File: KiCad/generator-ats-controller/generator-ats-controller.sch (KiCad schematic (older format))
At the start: 20 parts

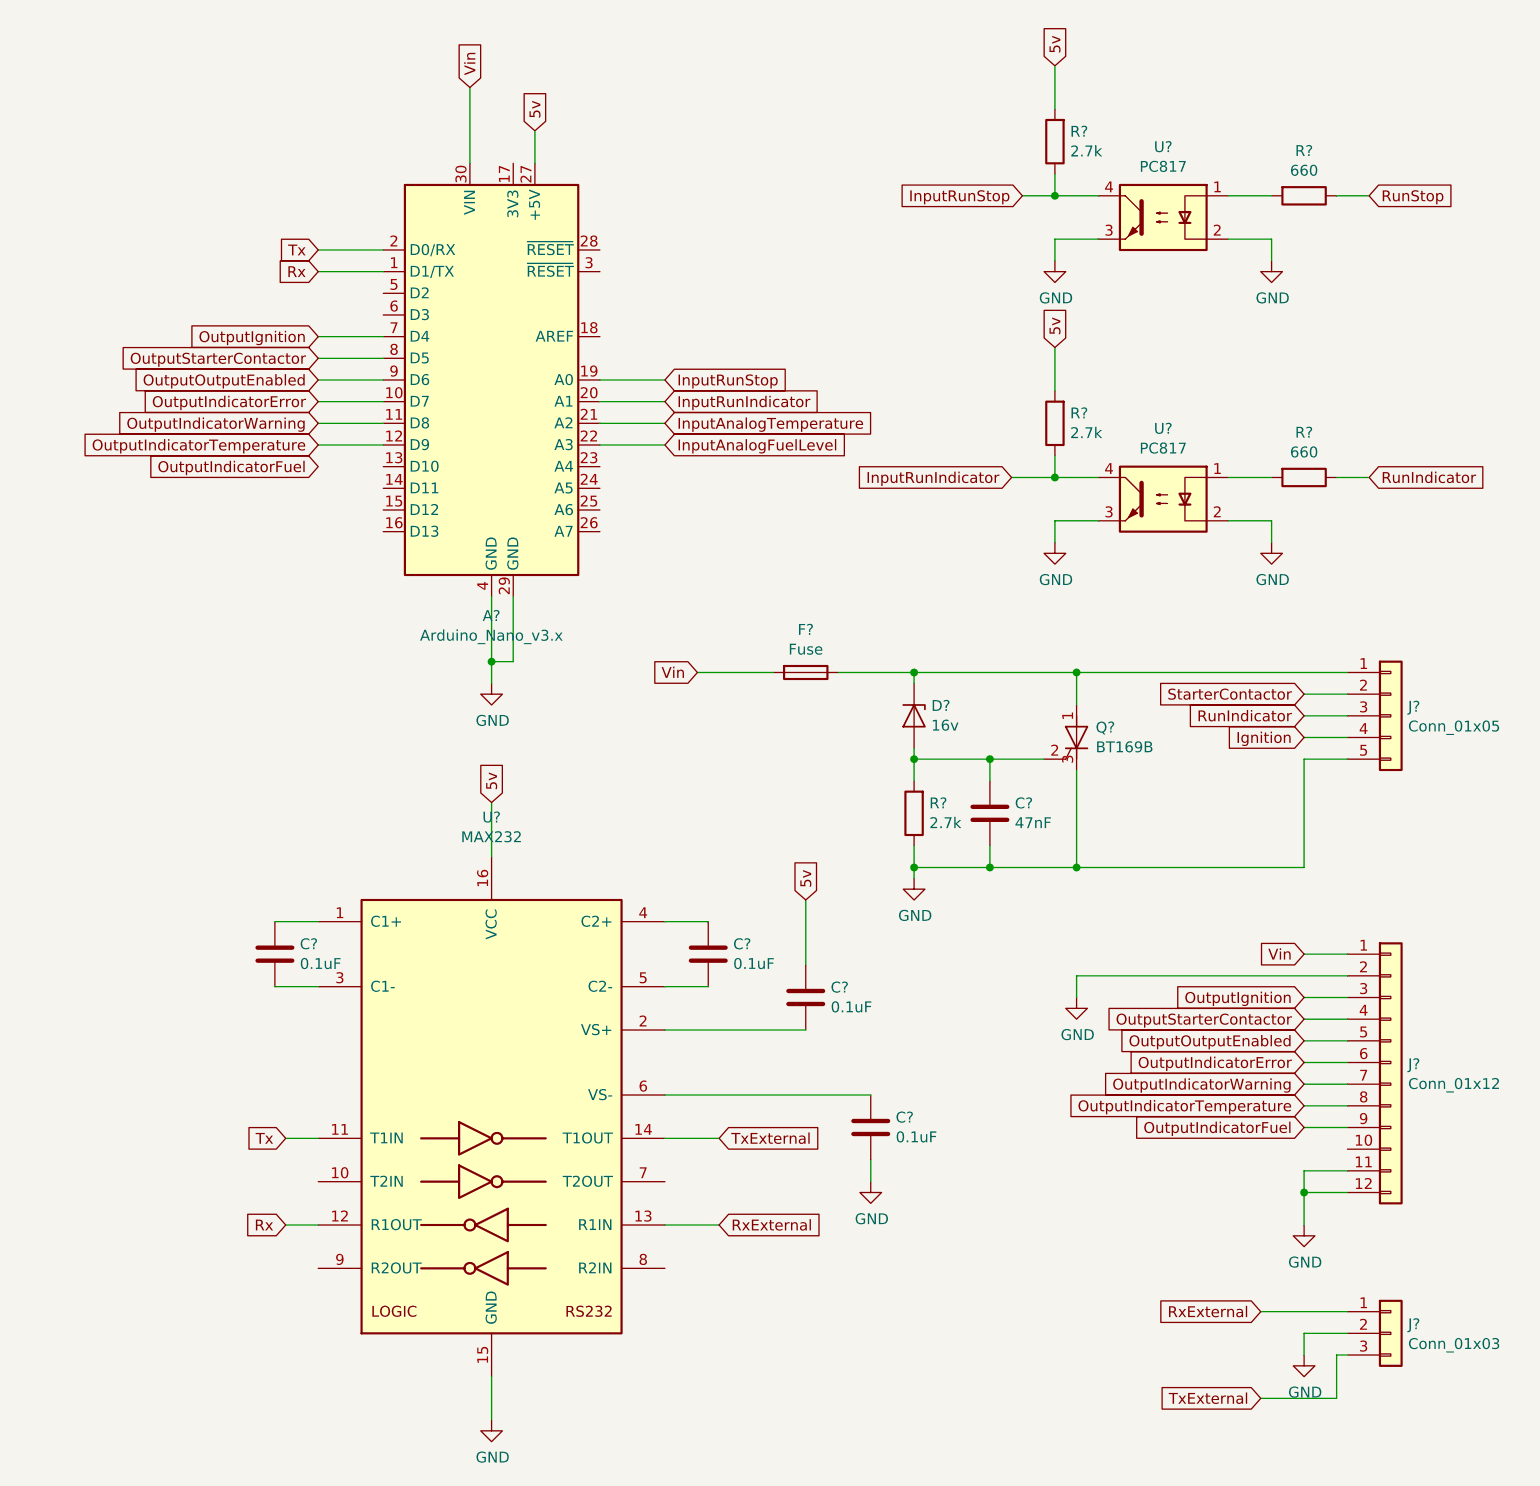
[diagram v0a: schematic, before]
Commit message: * Correct errors in schematic, largely around the MAX232
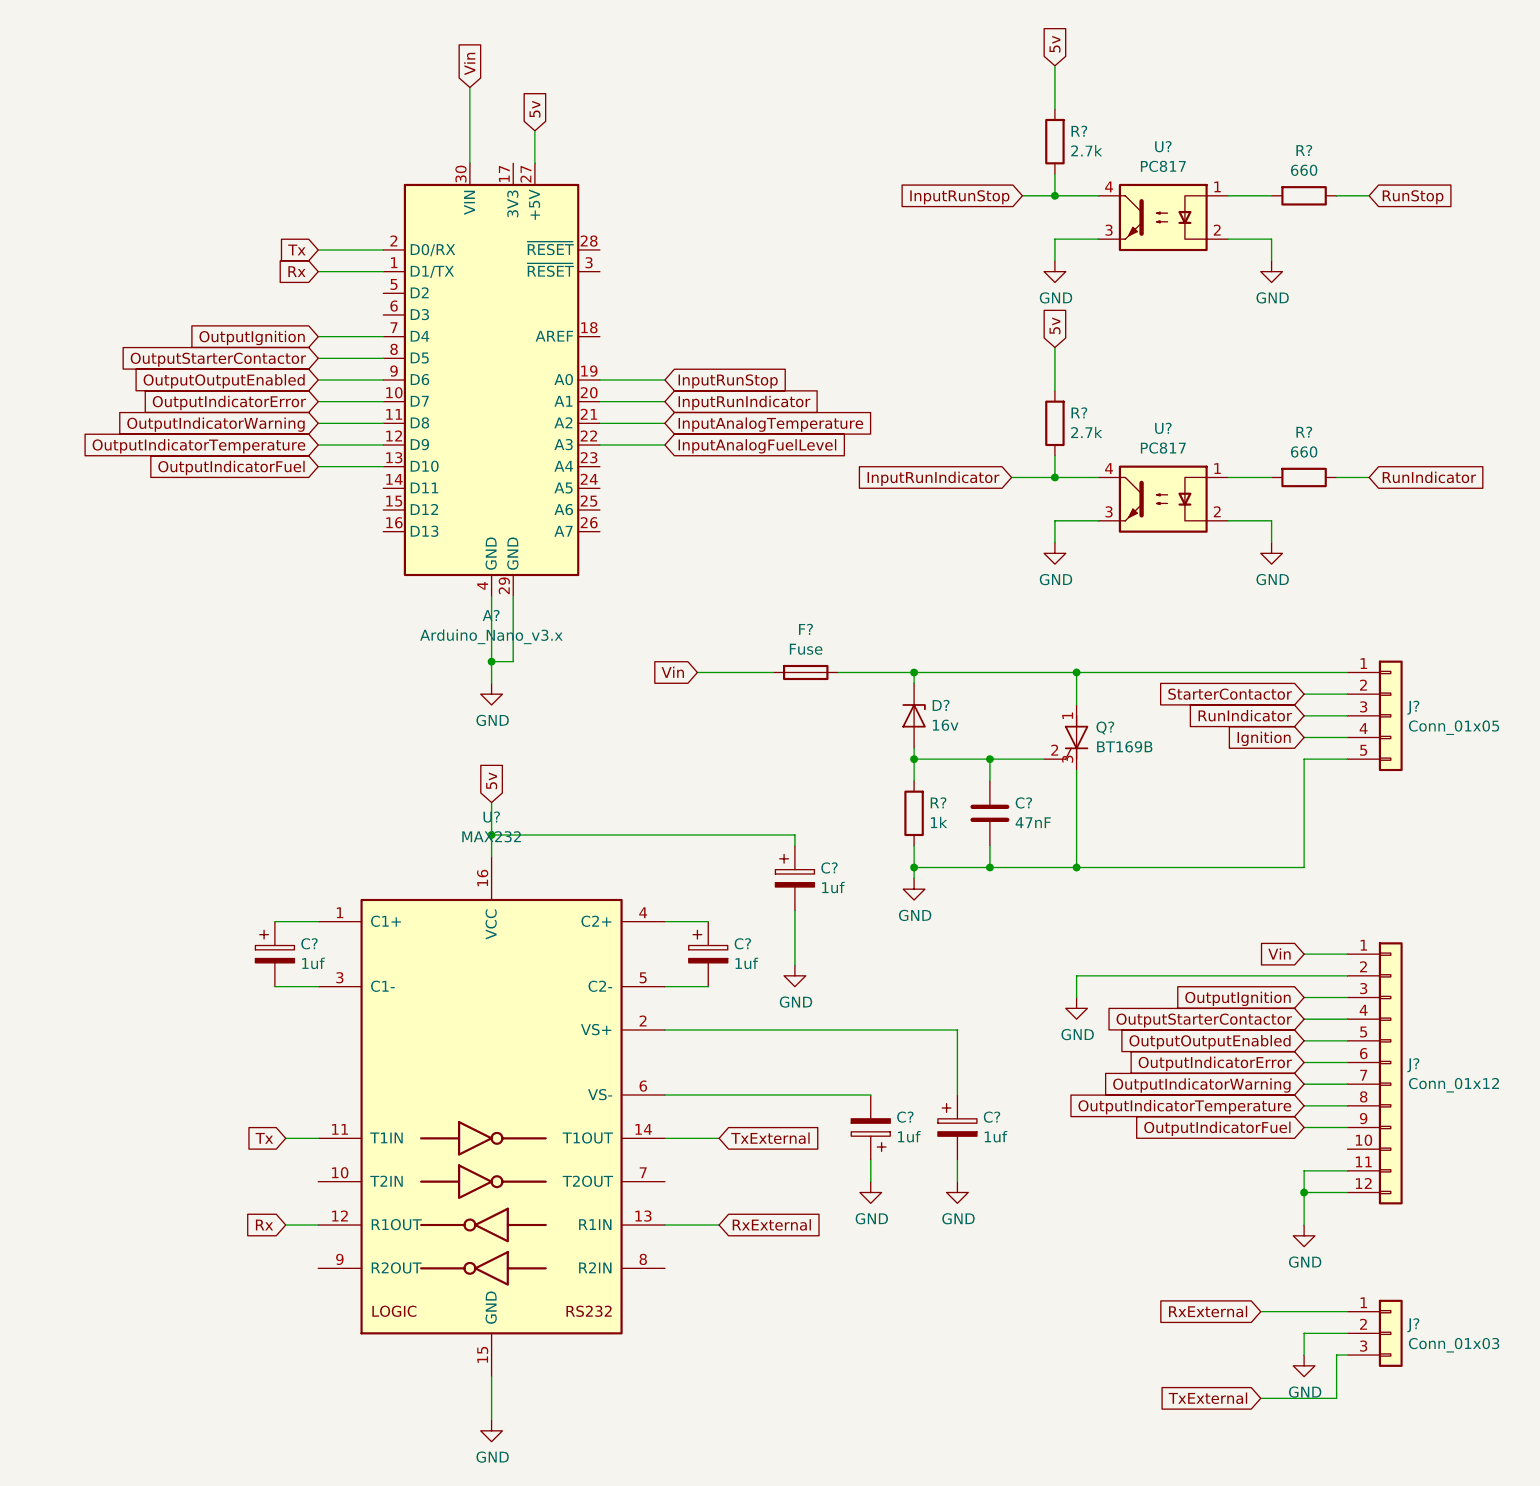
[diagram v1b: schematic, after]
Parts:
- removed C? (x4): 0.1uF, symbol Device:C
- added C? (x5): 1uf, symbol Device:CP
- R?: value 2.7k -> 1k
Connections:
- net 5v: now also C?.1
- net GND: now also C?.1, C?.2, C?.2
- net OutputIndicatorFuel: now also A?.13 (D10)
- net at U?.1 (C1+): now also C?.1
- net at U?.2 (VS+): now also C?.1
- net at U?.3 (C1-): now also C?.2
- net at U?.4 (C2+): now also C?.1
- net at U?.5 (C2-): now also C?.2
- net at U?.6 (VS-): now also C?.2
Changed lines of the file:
@@
-	1    0    0    -1
-$EndComp
-$Comp
-L Device:C C?
-U 1 1 5F2662F8
-P 1550 5100
-F 0 "C?" H 1665 5146 50  0000 L CNN
-F 1 "0.1uF" H 1665 5055 50  0000 L CNN
-F 2 "" H 1588 4950 50  0001 C CNN
-F 3 "~" H 1550 5100 50  0001 C CNN
-	1    1550 5100
-	1    0    0    -1
-$EndComp
-$Comp
-L Device:C C?
-U 1 1 5F2691ED
-P 3550 5100
-F 0 "C?" H 3665 5146 50  0000 L CNN
-F 1 "0.1uF" H 3665 5055 50  0000 L CNN
-F 2 "" H 3588 4950 50  0001 C CNN
-F 3 "~" H 3550 5100 50  0001 C CNN
-	1    3550 5100
-	1    0    0    -1
-$EndComp
-$Comp
-L Device:C C?
-U 1 1 5F269678
-P 4000 5300
-F 0 "C?" H 4115 5346 50  0000 L CNN
-F 1 "0.1uF" H 4115 5255 50  0000 L CNN
-F 2 "" H 4038 5150 50  0001 C CNN
-F 3 "~" H 4000 5300 50  0001 C CNN
-	1    4000 5300
-	1    0    0    -1
-$EndComp
-$Comp
-L Device:C C?
-U 1 1 5F269EC4
-P 4300 5900
-F 0 "C?" H 4415 5946 50  0000 L CNN
-F 1 "0.1uF" H 4415 5855 50  0000 L CNN
-F 2 "" H 4338 5750 50  0001 C CNN
-F 3 "~" H 4300 5900 50  0001 C CNN
-	1    4300 5900
 	1    0    0    -1
 $EndComp
@@
 Wire Wire Line
 	2450 1450 2450 1100
-Text GLabel 4000 4850 1    50   Input ~ 0
-5v
 $Comp
 L power:GND #PWR?
@@
 	1    0    0    -1
 $EndComp
-Wire Wire Line
-	3350 5450 4000 5450
 Text GLabel 1750 1850 0    50   Input ~ 0
 Tx
@@
 5v
 Wire Wire Line
-	2550 4400 2550 4650
+	2550 4400 2550 4550
 Wire Wire Line
 	6100 7150 6450 7150
@@
 P 4500 4450
 F 0 "R?" H 4430 4404 50  0000 R CNN
-F 1 "2.7k" H 4430 4495 50  0000 R CNN
+F 1 "1k" H 4430 4495 50  0000 R CNN
 F 2 "" V 4430 4450 50  0001 C CNN
 F 3 "~" H 4500 4450 50  0001 C CNN
@@
 Wire Wire Line
 	4850 4200 5100 4200
-Wire Wire Line
-	4000 4850 4000 5150
 $Comp
 L Connector_Generic:Conn_01x03 J?
@@
 Text GLabel 6100 6750 0    50   Input ~ 0
 RxExternal
+$Comp
+L power:GND #PWR?
+U 1 1 5F4B4680
+P 4700 6150
+F 0 "#PWR?" H 4700 5900 50  0001 C CNN
+F 1 "GND" H 4705 5977 50  0000 C CNN
+F 2 "" H 4700 6150 50  0001 C CNN
+F 3 "" H 4700 6150 50  0001 C CNN
+	1    4700 6150
+	1    0    0    -1
+$EndComp
+Wire Wire Line
+	4700 6150 4700 6050
+Wire Wire Line
+	4700 5750 4700 5450
+Wire Wire Line
+	3350 5450 4700 5450
+$Comp
+L Device:CP C?
+U 1 1 5F4BEB4E
+P 1550 5100
+F 0 "C?" H 1668 5146 50  0000 L CNN
+F 1 "1uf" H 1668 5055 50  0000 L CNN
+F 2 "" H 1588 4950 50  0001 C CNN
+F 3 "~" H 1550 5100 50  0001 C CNN
+	1    1550 5100
+	1    0    0    -1
+$EndComp
+$Comp
+L Device:CP C?
+U 1 1 5F4C0CED
+P 3550 5100
+F 0 "C?" H 3668 5146 50  0000 L CNN
+F 1 "1uf" H 3668 5055 50  0000 L CNN
+F 2 "" H 3588 4950 50  0001 C CNN
+F 3 "~" H 3550 5100 50  0001 C CNN
+	1    3550 5100
+	1    0    0    -1
+$EndComp
+$Comp
+L Device:CP C?
+U 1 1 5F4C10F1
+P 4700 5900
+F 0 "C?" H 4818 5946 50  0000 L CNN
+F 1 "1uf" H 4818 5855 50  0000 L CNN
+F 2 "" H 4738 5750 50  0001 C CNN
+F 3 "~" H 4700 5900 50  0001 C CNN
+	1    4700 5900
+	1    0    0    -1
+$EndComp
+$Comp
+L Device:CP C?
+U 1 1 5F4C1502
+P 4300 5900
+F 0 "C?" H 4182 5854 50  0000 R CNN
+F 1 "1uf" H 4182 5945 50  0000 R CNN
+F 2 "" H 4338 5750 50  0001 C CNN
+F 3 "~" H 4300 5900 50  0001 C CNN
+	1    4300 5900
+	-1   0    0    1
+$EndComp
+$Comp
+L Device:CP C?
+U 1 1 5F4C6ED9
+P 3950 4750
+F 0 "C?" H 4068 4796 50  0000 L CNN
+F 1 "1uf" H 4068 4705 50  0000 L CNN
+F 2 "" H 3988 4600 50  0001 C CNN
+F 3 "~" H 3950 4750 50  0001 C CNN
+	1    3950 4750
+	1    0    0    -1
+$EndComp
+Wire Wire Line
+	2550 4550 3950 4550
+Wire Wire Line
+	3950 4550 3950 4600
+Connection ~ 2550 4550
+Wire Wire Line
+	2550 4550 2550 4650
+$Comp
+L power:GND #PWR?
+U 1 1 5F4CAC20
+P 3950 5150
+F 0 "#PWR?" H 3950 4900 50  0001 C CNN
+F 1 "GND" H 3955 4977 50  0000 C CNN
+F 2 "" H 3950 5150 50  0001 C CNN
+F 3 "" H 3950 5150 50  0001 C CNN
+	1    3950 5150
+	1    0    0    -1
+$EndComp
+Wire Wire Line
+	3950 4900 3950 5150
+Wire Wire Line
+	2050 2850 1750 2850
 $EndSCHEMATC
